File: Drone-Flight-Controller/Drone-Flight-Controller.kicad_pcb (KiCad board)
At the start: 4 copper layers, 30 x 65 mm, 52 parts, among them J1 Screw_Terminal_01x02, J10 Conn_ARM_SWD_TagConnect_TC203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, J2 USB_B_Micro, J3 TestPoint, J4 TestPoint, J5 TestPoint, J6 TestPoint, J7 TestPoint, J8 TestPoint, J9 Raspberry_Pi_4, U1 LMR51430, U4 USBLC6-2SC6, U5 ADC101C021CIMK, U6 MPU-6050, U7 BMP280, U8 STM32F413ZHJx, Y1 16MHz

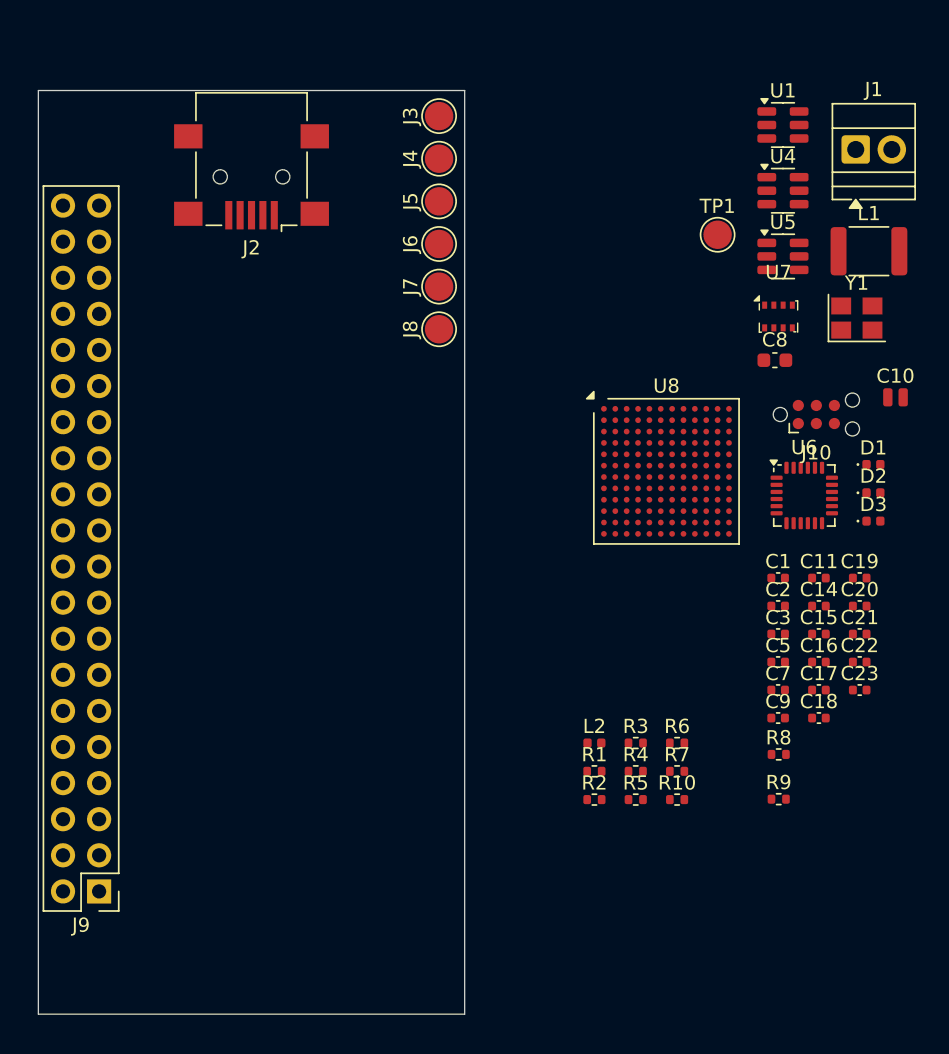
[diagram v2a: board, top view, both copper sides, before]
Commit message: laid out pcb with new mcu
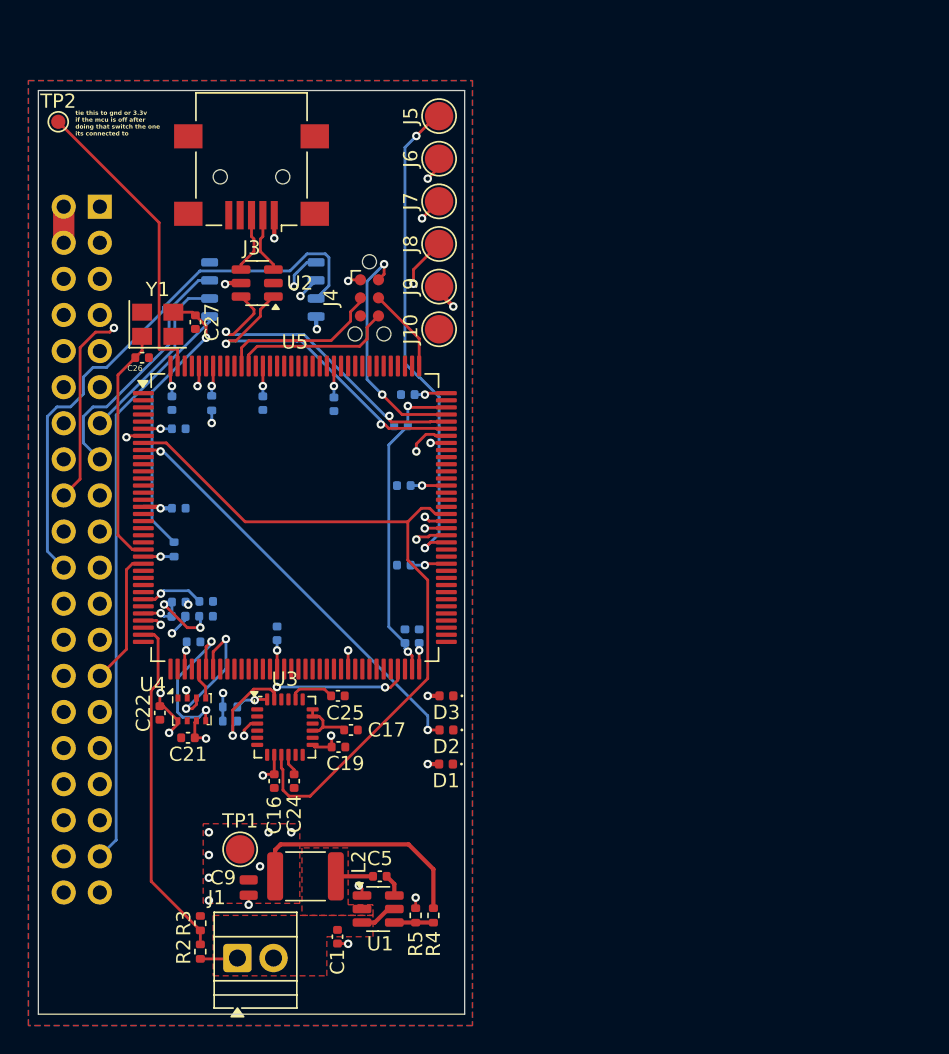
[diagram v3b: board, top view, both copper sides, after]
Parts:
- removed the C1 at (64.3, 46.5)
- removed the C3 at (64.3, 50.5)
- removed the C9 at (64.3, 56.4)
- removed the R1 at (51.3, 60.1)
- removed the R6 at (57.1, 58.1)
- removed the R7 at (57.1, 60.1)
- removed U8: STM32F413ZHJx, Package_BGA:UFBGA-144_10x10mm_Layout12x12_P0.8mm
- added C10: 100n, Capacitor_SMD:C_0402_1005Metric, B.Cu at (37.9, 45.6)
- added C12: 100n, Capacitor_SMD:C_0402_1005Metric, B.Cu at (22.1, 36.0)
- added C13: 100n, Capacitor_SMD:C_0402_1005Metric, B.Cu at (38.2, 33.6)
- added C15: 100n, Capacitor_SMD:C_0402_1005Metric, B.Cu at (37.9, 40.0)
- added C18: 100n, Capacitor_SMD:C_0402_1005Metric, B.Cu at (23.1, 51.0)
- added C20: 100n, Capacitor_SMD:C_0402_1005Metric, B.Cu at (29.0, 50.4)
- added C23: 4.3uF, Capacitor_SMD:C_0402_1005Metric, B.Cu at (24.0, 48.1)
- added C26: 12p, Capacitor_SMD:C_0402_1005Metric, F.Cu at (19.5, 31.0)
- added C27: 12p, Capacitor_SMD:C_0402_1005Metric, F.Cu at (23.2, 28.5)
- added C29: 2.2uF, Capacitor_SMD:C_0402_1005Metric, B.Cu at (37.7, 35.8)
- added C6: 100n, Capacitor_SMD:C_0402_1005Metric, B.Cu at (21.6, 34.2)
- added C7: 100n, Capacitor_SMD:C_0402_1005Metric, B.Cu at (28.0, 34.2)
- added R8: 47, Resistor_SMD:R_0402_1005Metric, B.Cu at (21.8, 44.5)
- added TP2: TestPoint, TestPoint:TestPoint_Pad_D1.0mm, F.Cu at (13.6, 14.4)
- added U3: MPU-9150, Sensor_Motion:InvenSense_QFN-24_4x4mm_P0.5mm, F.Cu at (29.6, 57.0)
- C11, C14: moved to B.Cu
- C2: renamed from C15; moved to B.Cu
- C28: renamed from C5; moved to B.Cu
- C3: renamed from C16; moved to B.Cu
- C8: value 4u7 -> 100n; footprint Capacitor_SMD:C_0603_1608Metric -> Capacitor_SMD:C_0402_1005Metric; moved to B.Cu
- J2: renamed from J9; moved to B.Cu
- L1: renamed from L2; moved to B.Cu
- R1: renamed from R10; moved to B.Cu
- R6: renamed from R8; moved to B.Cu
- R7: renamed from R9; moved to B.Cu
- U5: value ADC101C021CIMK -> STM32F413ZHTx; footprint Package_TO_SOT_SMD:SOT-23-6 -> Package_QFP:LQFP-144_20x20mm_P0.5mm
- U6: value MPU-6050 -> XTSD08G; footprint Sensor_Motion:InvenSense_QFN-24_4x4mm_P0.5mm -> Package_LGA:LGA-8_8x6mm_P1.27mm; moved to B.Cu
- moved J1 71.6 mm to (26.2, 73.2)
- moved U1 62.1 mm to (36.1, 69.8)
- moved L2 59.2 mm to (31.0, 67.5), turned to 180 degrees
- moved C9 57.1 mm to (27.0, 68.3), turned to -90 degrees
- moved TP1 54.8 mm to (26.4, 65.6)
- moved U4 49.7 mm to (23.0, 55.8)
- moved C22 49.3 mm to (20.8, 56.0), turned to 90 degrees
- moved Y1 49.2 mm to (20.6, 28.6)
- moved J2 48.2 mm to (16.5, 20.4)
- moved C21 47.6 mm to (22.7, 57.8), turned to 180 degrees
- moved C11 45.3 mm to (22.1, 41.6)
- moved C2 45.1 mm to (22.1, 48.2)
- moved C3 43.3 mm to (24.0, 49.2)
- moved R1 43.0 mm to (24.4, 34.2), turned to 90 degrees
- moved C24 41.7 mm to (30.2, 60.8), turned to 90 degrees
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- renumbered C2 to C1, C17 to C16, C18 to C17, C22 to C21, C23 to C22, C20 to C24, C21 to C25, C7 to C5, C10 to C9, D3 to D2, D2 to D3, J8 to J10, J2 to J3, J10 to J4, J3 to J5, J4 to J6, J5 to J7, J6 to J8, J7 to J9, L1 to L2, R4 to R2, R5 to R3, R2 to R4, R3 to R5, U4 to U2, U7 to U4
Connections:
- C17 pad 1: Net-(U6-GND) -> Net-(C17-Pad1)
- C24 pad 2: Net-(U6-REGOUT) -> Net-(U3-REGOUT)
- C25 pad 1: Net-(U6-CPOUT) -> Net-(U3-CPOUT)
- C28 pad 2: unconnected-(C5-Pad2) -> Net-(U5-VCAP_1)
- J2 pad 13: unconnected-(J9-GPIO27/SDIO_DAT3-Pad13) -> SD_CARD_DAT3
- J2 pad 15: unconnected-(J9-GPIO22/SDIO_CLK-Pad15) -> SD_CARD_CLK
- J2 pad 16: unconnected-(J9-GPIO23/SDIO_CMD-Pad16) -> SD_CARD_CMD
- J2 pad 18: unconnected-(J9-GPIO24/SDIO_DAT0-Pad18) -> SD_CARD_DAT0
- J2 pad 22: unconnected-(J9-GPIO25/SDIO_DAT1-Pad22) -> SD_CARD_DAT1
- J2 pad 27: unconnected-(J9-ID_SD_I2C0/GPIO00-Pad27) -> NRST
- J2 pad 37: unconnected-(J9-GPIO26/SDIO_DAT2-Pad37) -> SD_CARD_DAT2
- R2 pad 2: Net-(U5-V_{IN}) -> BATVOLTAGE
- R3 pad 1: Net-(U5-V_{IN}) -> BATVOLTAGE
- U5 pad 1: +3.3V -> unconnected-(U5-PE2-Pad1)
- U5 pad 2: GND -> unconnected-(U5-PE3-Pad2)
- U5 pad 3: Net-(U5-V_{IN}) -> unconnected-(U5-PE4-Pad3)
- U5 pad 4: BATVOLTAGE_ADDR -> unconnected-(U5-PE5-Pad4)
- U5 pad 5: BATVOLTAGE_SCL -> unconnected-(U5-PE6-Pad5)
- U5 pad 6: BATVOLTAGE_SDA -> +3.3V
- U6 pad 1: unconnected-(U6-CLKIN-Pad1) -> SD_CARD_DAT2
- U6 pad 2: unconnected-(U6-NC-Pad2) -> SD_CARD_DAT3
- U6 pad 3: unconnected-(U6-NC-Pad3) -> SD_CARD_CLK
- U6 pad 4: unconnected-(U6-NC-Pad4) -> GND
- U6 pad 5: unconnected-(U6-NC-Pad5) -> SD_CARD_CMD
- U6 pad 6: unconnected-(U6-AUX_DA-Pad6) -> SD_CARD_DAT0
- U6 pad 7: unconnected-(U6-AUX_CL-Pad7) -> SD_CARD_DAT1
- Y1 pad 1: Net-(C1-Pad1) -> Net-(U5-PH0)
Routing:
- net IMU_ADDR: track 0.00 -> 52.1 mm
- net +3.3V: track 0.00 -> 49.8 mm, vias 0 -> 26
- net SD_CARD_DAT2: track 0.00 -> 41.2 mm
- net SD_CARD_DAT1: track 0.00 -> 39.9 mm
- net +5V: track 0.00 -> 37.2 mm, vias 0 -> 11
- net PWM_0: track 0.00 -> 34.6 mm, vias 0 -> 2
- net PWM_1: track 0.00 -> 31.6 mm, vias 0 -> 2
- net SD_CARD_CMD: track 0.00 -> 31.3 mm, vias 0 -> 1
- net UART_RX: track 0.00 -> 30.7 mm, vias 0 -> 1
- net UART_TX: track 0.00 -> 30.7 mm, vias 0 -> 1
- net LED_STATUS: track 0.00 -> 29.6 mm, vias 0 -> 2
- net SD_CARD_DAT0: track 0.00 -> 29.4 mm, vias 0 -> 2
- net IMU_SDA: track 0.00 -> 27.5 mm, vias 0 -> 2
- net PWM_2: track 0.00 -> 26.3 mm, vias 0 -> 2
- net BATVOLTAGE: track 0.00 -> 24.3 mm
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- added copper zone on F.Cu, net +12V
- added copper zone on In1.Cu, net +3.3V
- added copper zone on F.Cu, net +5V
- added copper zone on In2.Cu, net +5V
- added copper zone on B.Cu, net GND
- added copper zone on F.Cu, net GND
- added copper zone on F.Cu, net Net-(U1-SW)
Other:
- board text added: "tie this to gnd or 3.3v if the mcu is off after doing that switch the one its connected to"

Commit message: remove stm32
processing will be done on the rpi now
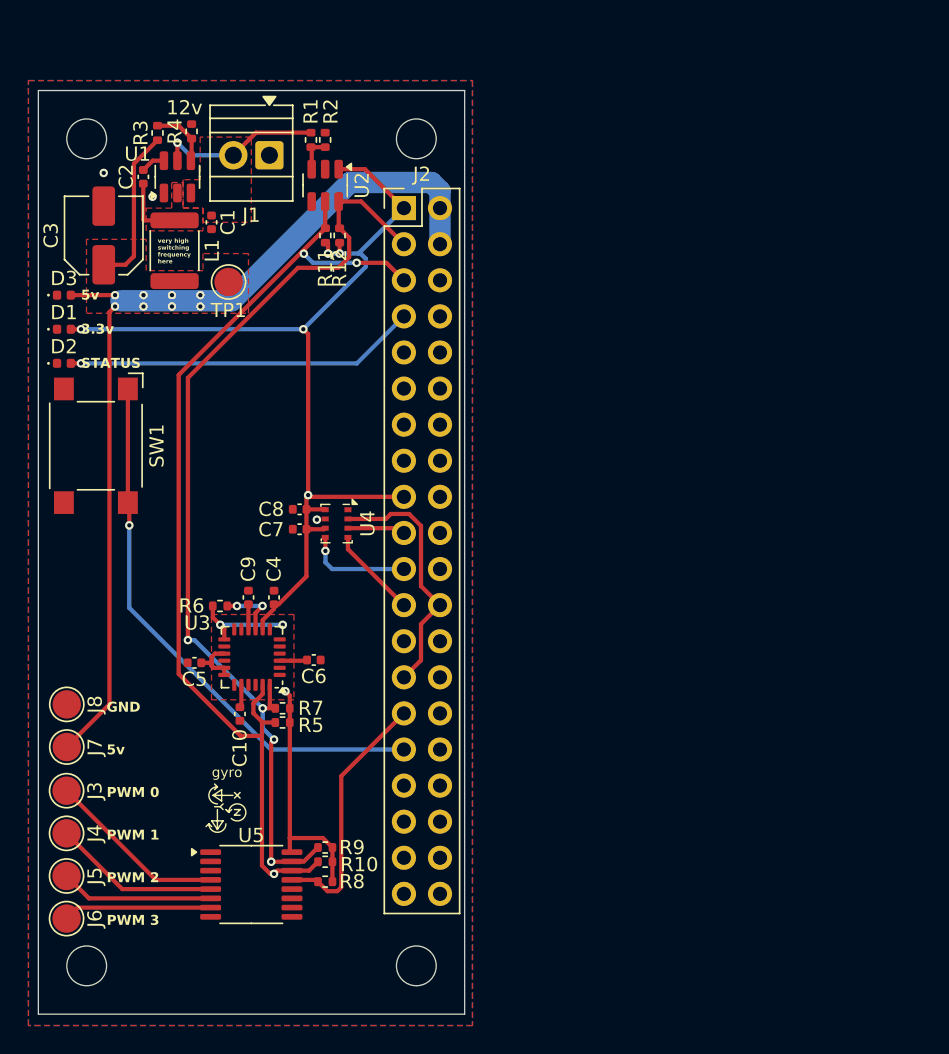
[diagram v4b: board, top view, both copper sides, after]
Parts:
- removed C11, C12, C13, C14, C15, C18, C20: 100n, Capacitor_SMD:C_0402_1005Metric
- removed C16: 10nF, Capacitor_SMD:C_0402_1005Metric
- removed C17, C25: 2.2nF, Capacitor_SMD:C_0402_1005Metric
- removed C19, C24: 0.1uF, Capacitor_SMD:C_0402_1005Metric
- removed C21, C22: 100nF, Capacitor_SMD:C_0402_1005Metric
- removed C23: 4.3uF, Capacitor_SMD:C_0402_1005Metric
- removed C26, C27: 12p, Capacitor_SMD:C_0402_1005Metric
- removed C28, C29: 2.2uF, Capacitor_SMD:C_0402_1005Metric
- removed J10, J9: TestPoint, TestPoint:TestPoint_Pad_D2.0mm
- removed L2: 6.8uH, Inductor_SMD:L_1812_4532Metric
- removed TP2: TestPoint, TestPoint:TestPoint_Pad_D1.0mm
- removed U6: XTSD08G, Package_LGA:LGA-8_8x6mm_P1.27mm
- removed Y1: 16MHz, Crystal:Crystal_SMD_3225-4Pin_3.2x2.5mm
- added C4: 10nF, Capacitor_SMD:C_0402_1005Metric, F.Cu at (28.8, 47.9)
- added R10: 10kOhm, Resistor_SMD:R_0402_1005Metric, F.Cu at (32.4, 66.5)
- added R11: 10kOhm, Resistor_SMD:R_0402_1005Metric, F.Cu at (32.4, 22.4)
- added R12: 10kOhm, Resistor_SMD:R_0402_1005Metric, F.Cu at (33.4, 22.4)
- added R9: 10kOhm, Resistor_SMD:R_0402_1005Metric, F.Cu at (32.4, 65.5)
- added SW1: SW_Omron_B3FS, Button_Switch_SMD:SW_SPST_Omron_B3FS-100xP, F.Cu at (16.2, 37.2)
- C10: value 100n -> 2.2nF; moved to F.Cu
- C2: value 1u -> 0.1uF; moved to F.Cu
- C3: value 10n -> 33uF; footprint Capacitor_SMD:C_0402_1005Metric -> Capacitor_SMD:C_Elec_5x5.4; moved to F.Cu
- C5: value 0.1uF -> 2.2nF
- C6: value 100n -> 0.1uF; moved to F.Cu
- C7, C8: value 100n -> 100nF; moved to F.Cu
- C9: value 33uF -> 0.1uF; footprint Capacitor_SMD:C_0504_1310Metric -> Capacitor_SMD:C_0402_1005Metric
- J2, R6, R7: moved to F.Cu
- J3: value USB_B_Micro -> TestPoint; footprint Connector_USB:USB_Mini-B_Lumberg_2486_01_Horizontal -> TestPoint:TestPoint_Pad_D2.0mm
- J4: value Conn_ARM_SWD_TagConnect_TC2030-NL -> TestPoint; footprint Connector:Tag-Connect_TC2030-IDC-NL_2x03_P1.27mm_Vertical -> TestPoint:TestPoint_Pad_D2.0mm
- L1: value 39n -> 6.8uH; footprint Inductor_SMD:L_0402_1005Metric -> Inductor_SMD:L_1812_4532Metric; moved to F.Cu
- R1: value 10k -> 1.5kOhm; moved to F.Cu
- R2: value 1.5kOhm -> 1kOhm
- R3: value 1kOhm -> 100kOhm
- R4: value 100kOhm -> 13.7kOhm
- R5: value 13.7kOhm -> 10kOhm
- R8: value 47 -> 10kOhm; moved to F.Cu
- U2: value USBLC6-2SC6 -> ADC101C021CIMK
- U5: value STM32F413ZHTx -> PCA9531PW; footprint Package_QFP:LQFP-144_20x20mm_P0.5mm -> Package_SO:TSSOP-16_4.4x5mm_P0.65mm
- moved J5 59.6 mm to (14.2, 67.5), turned to -90 degrees
- moved J6 59.6 mm to (14.2, 70.5), turned to -90 degrees
- moved R2 57.8 mm to (32.4, 15.7)
- moved R4 57.7 mm to (23.0, 15.1), turned to 90 degrees
- moved J1 56.5 mm to (28.5, 16.8), turned to 180 degrees
- moved R3 55.7 mm to (20.6, 15.2)
- moved U1 53.4 mm to (22.0, 18.3), turned to 90 degrees
- moved C1 51.1 mm to (24.4, 21.5)
- moved J7 46.5 mm to (14.2, 58.4), turned to -90 degrees
- moved J3 45.1 mm to (14.2, 61.5), turned to -90 degrees
- moved J4 43.3 mm to (14.2, 64.5)
- moved J8 41.7 mm to (14.2, 55.4), turned to -90 degrees
- moved D1 40.7 mm to (14.0, 29.0), turned to 0 degrees
- moved TP1 39.9 mm to (25.6, 25.7), turned to 180 degrees
- moved D3 39.0 mm to (14.0, 26.6), turned to 0 degrees
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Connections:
- C10 pad 1: +3.3V -> Net-(U3-CPOUT)
- C2 pad 1: +3.3VA -> Net-(U1-CB)
- C2 pad 2: GND -> Net-(U1-SW)
- C3 pad 1: +3.3VA -> +5V
- C5 pad 1: Net-(U1-CB) -> Net-(C5-Pad1)
- C5 pad 2: Net-(U1-SW) -> GND
- C6 pad 1: +3.3V -> GND
- C6 pad 2: GND -> +3.3V
- C8 pad 1: +3.3V -> GND
- C8 pad 2: GND -> +3.3V
- C9 pad 1: +5V -> GND
- C9 pad 2: GND -> Net-(U3-REGOUT)
- J1 pad 1: +12V -> GND
- J1 pad 2: GND -> +12V
- J2 pad 10: UART_RX -> unconnected-(J2-GPIO15/UART_RXD-Pad10)
- J2 pad 13: SD_CARD_DAT3 -> unconnected-(J2-GPIO27/SDIO_DAT3-Pad13)
- J2 pad 15: SD_CARD_CLK -> unconnected-(J2-GPIO22/SDIO_CLK-Pad15)
- J2 pad 16: SD_CARD_CMD -> unconnected-(J2-GPIO23/SDIO_CMD-Pad16)
- J2 pad 18: SD_CARD_DAT0 -> unconnected-(J2-GPIO24/SDIO_DAT0-Pad18)
- J2 pad 19: unconnected-(J2-MOSI_SPI0/GPIO10-Pad19) -> BAROMETER_SDI
- J2 pad 21: unconnected-(J2-MISO_SPI0/GPIO09-Pad21) -> BAROMETER_SDO
- J2 pad 22: SD_CARD_DAT1 -> unconnected-(J2-GPIO25/SDIO_DAT1-Pad22)
- J2 pad 23: unconnected-(J2-SCLK_SPI0/GPIO11-Pad23) -> BAROMETER_SCK
- J2 pad 24: unconnected-(J2-~{CE0}_SPI0/GPIO08-Pad24) -> BAROMETER_CSB
- J2 pad 27: NRST -> BAROMETER_CSB
- J2 pad 28: unconnected-(J2-ID_SC_I2C0/GPIO01-Pad28) -> IMU_ADDR
- J2 pad 29: unconnected-(J2-GPCLK1/GPIO05-Pad29) -> PWM_RESET
- J2 pad 3: unconnected-(J2-SDA_I2C1/GPIO02-Pad3) -> I2C_SDA
- J2 pad 31: unconnected-(J2-GPCLK2/GPIO06-Pad31) -> Net-(J2-GPCLK2/GPIO06)
- J2 pad 37: SD_CARD_DAT2 -> unconnected-(J2-GPIO26/SDIO_DAT2-Pad37)
- J2 pad 5: unconnected-(J2-SCL_I2C1/GPIO03-Pad5) -> I2C_SCL
- J2 pad 7: unconnected-(J2-GPCLK0/GPIO04-Pad7) -> LED_STATUS
- J2 pad 8: UART_TX -> unconnected-(J2-GPIO14/UART_TXD-Pad8)
- J3 pad 1: +5V -> PWM_0
- J4 pad 1: +3.3V -> PWM_1
- J5 pad 1: PWM_0 -> PWM_2
- J6 pad 1: PWM_1 -> PWM_3
- J7 pad 1: PWM_2 -> +5V
- J8 pad 1: PWM_3 -> GND
- L1 pad 1: +3.3V -> Net-(U1-SW)
- L1 pad 2: +3.3VA -> +5V
- R1 pad 1: +3.3V -> +12V
- R1 pad 2: BOOT0 -> BATVOLTAGE
- R2 pad 1: +12V -> BATVOLTAGE
- R2 pad 2: BATVOLTAGE -> GND
- R3 pad 1: BATVOLTAGE -> +5V
- R3 pad 2: GND -> Net-(U1-FB)
- R4 pad 1: +5V -> Net-(U1-FB)
- R4 pad 2: Net-(U1-FB) -> GND
- R5 pad 1: Net-(U1-FB) -> +3.3V
- R5 pad 2: GND -> I2C_SCL
- R6 pad 1: +3.3V -> Net-(U3-AD0)
- R6 pad 2: IMU_SCL -> +3.3V
- R7 pad 2: IMU_SDA -> I2C_SDA
- R8 pad 1: Net-(U5-PH1) -> +3.3V
- R8 pad 2: Net-(C27-Pad1) -> PWM_RESET
- U2 pad 1: USB_D- -> +3.3V
- U2 pad 3: USB_CONN_D- -> BATVOLTAGE
- U2 pad 4: USB_CONN_D+ -> GND
- U2 pad 5: +5V -> I2C_SCL
- U2 pad 6: USB_D+ -> I2C_SDA
- U3 pad 15: Net-(C17-Pad1) -> Net-(C5-Pad1)
- U3 pad 17: Net-(C17-Pad1) -> Net-(C5-Pad1)
- U3 pad 18: Net-(C17-Pad1) -> Net-(C5-Pad1)
- U3 pad 23: IMU_SCL -> I2C_SCL
- U3 pad 24: IMU_SDA -> I2C_SDA
- U3 pad 9: IMU_ADDR -> Net-(U3-AD0)
- U5 pad 1: unconnected-(U5-PE2-Pad1) -> GND
- U5 pad 13: unconnected-(U5-PF3-Pad13) -> PWM_RESET
- U5 pad 14: unconnected-(U5-PF4-Pad14) -> I2C_SCL
- U5 pad 15: unconnected-(U5-PF5-Pad15) -> I2C_SDA
- U5 pad 16: GND -> +3.3V
- U5 pad 2: unconnected-(U5-PE3-Pad2) -> GND
- U5 pad 3: unconnected-(U5-PE4-Pad3) -> GND
- U5 pad 4: unconnected-(U5-PE5-Pad4) -> PWM_0
- U5 pad 5: unconnected-(U5-PE6-Pad5) -> PWM_1
- U5 pad 6: +3.3V -> PWM_2
- U5 pad 7: BAROMETER_CSB -> PWM_3
- U5 pad 8: IMU_ADDR -> GND
- U5 pad 9: LED_STATUS -> unconnected-(U5-LED4-Pad9)
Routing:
- net I2C_SCL: track 0.00 -> 71.9 mm, vias 0 -> 3
- net I2C_SDA: track 0.00 -> 68.2 mm, vias 0 -> 4
- net IMU_ADDR: track 52.1 -> 0.00 mm
- net +3.3V: track 49.8 -> 96.4 mm, vias 26 -> 8
- net SD_CARD_DAT2: track 41.2 -> 0.00 mm
- net SD_CARD_DAT1: track 39.9 -> 0.00 mm
- net +5V: track 37.2 -> 76.7 mm, vias 11 -> 8
- net Net-(J2-GPCLK2/GPIO06): track 0.00 -> 38.9 mm, vias 0 -> 1
- net SD_CARD_CMD: track 31.3 -> 0.00 mm, vias 1 -> 0
- net UART_RX: track 30.7 -> 0.00 mm, vias 1 -> 0
- net UART_TX: track 30.7 -> 0.00 mm, vias 1 -> 0
- net SD_CARD_DAT0: track 29.4 -> 0.00 mm, vias 2 -> 0
- net IMU_SDA: track 27.5 -> 0.00 mm, vias 2 -> 0
- net USB_D-: track 23.3 -> 0.00 mm, vias 2 -> 0
- net USB_D+: track 22.6 -> 0.00 mm, vias 2 -> 0
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- added copper zone on F.Cu, net +3.3V
- removed copper zone on In1.Cu, net +3.3V
- removed copper zone on In2.Cu, net +5V
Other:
- outline, holes or cut-outs redrawn
- copper layers 4 -> 2
- board text added: "12v"
- board text added: "3.3v"
- board text added: "5v"
- board text added: "GND"
- board text added: "PWM 0"
- board text added: "PWM 1"
- board text added: "PWM 2"
- board text added: "PWM 3"
- board text added: "STATUS"
- board text added: "gyro"
- board text added: "very high switching frequency here"
- board text removed: "tie this to gnd or 3.3v if the mcu is off after doing that switch the one its connected to"

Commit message: pin header is female and on the bottom now
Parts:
- added J10: TestPoint, TestPoint:TestPoint_Pad_D2.0mm, F.Cu at (22.0, 75.2)
- added J11: TestPoint, TestPoint:TestPoint_Pad_D2.0mm, F.Cu at (25.0, 75.2)
- added J12: TestPoint, TestPoint:TestPoint_Pad_D2.0mm, F.Cu at (28.0, 75.2)
- added J9: TestPoint, TestPoint:TestPoint_Pad_D2.0mm, F.Cu at (19.0, 75.2)
- J2: footprint Connector_PinHeader_2.54mm:PinHeader_2x20_P2.54mm_Vertical -> Connector_PinSocket_2.54mm:PinSocket_2x20_P2.54mm_Vertical; moved to B.Cu
- turned J2 to 180 degrees
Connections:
- U5 pad 10: unconnected-(U5-LED5-Pad10) -> PWM_5
- U5 pad 11: unconnected-(U5-LED6-Pad11) -> PWM_6
- U5 pad 12: unconnected-(U5-LED7-Pad12) -> PWM_7
- U5 pad 9: unconnected-(U5-LED4-Pad9) -> PWM_4
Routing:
- net PWM_4: track 0.00 -> 13.1 mm
- net PWM_5: track 0.00 -> 12.8 mm
- net PWM_6: track 0.00 -> 11.4 mm
- net PWM_7: track 0.00 -> 9.88 mm
- net GND: vias 3 -> 12
- net +5V: vias 8 -> 11
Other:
- board text added: "0"
- board text added: "1"
- board text added: "2"
- board text added: "3"
- board text added: "4"
- board text added: "5"
- board text added: "6"
- board text added: "7"
- board text added: "PWM"
- board text removed: "PWM 0"
- board text removed: "PWM 1"
- board text removed: "PWM 2"
- board text removed: "PWM 3"

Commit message: change imu to one that isnt eol
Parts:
- removed the C10 at (26.4, 56.1)
- removed the C4 at (28.8, 47.9)
- removed the C5 at (23.2, 52.5)
- removed the R5 at (29.4, 56.7)
- removed the R6 at (25.0, 48.5)
- removed the U3 at (27.2, 52.1)
- added C2: 1uF, Capacitor_SMD:C_0402_1005Metric, F.Cu at (25.8, 45.4)
- added C3: 1uF, Capacitor_SMD:C_0402_1005Metric, F.Cu at (25.8, 47.4)
- added C7: 0.1uF, Capacitor_SMD:C_0402_1005Metric, F.Cu at (26.0, 54.8)
- added F1: Fuse, Fuse:Fuse_1206_3216Metric, F.Cu at (24.0, 8.80)
- added U1: MCP1700x-180xxMB, Package_TO_SOT_SMD:SOT-89-3, F.Cu at (29.2, 46.4)
- added U4: ICM-20948, Sensor_Motion:InvenSense_QFN-24_3x3mm_P0.4mm, F.Cu at (27.2, 52.1)
- moved C6 7.60 mm to (24.4, 49.8), turned to -90 degrees
- moved C9 6.46 mm to (24.4, 53.8)
- moved R7 6.31 mm to (24.4, 51.8), turned to 90 degrees
- moved R4 0.75 mm to (22.8, 15.8), turned to 0 degrees
- moved R3 0.69 mm to (20.9, 15.8), turned to 0 degrees
- moved C4 0.22 mm to (19.4, 18.4)
- moved U2 0.13 mm to (22.0, 18.4)
- moved C1 0.08 mm to (24.4, 21.4)
- renumbered C8 to C10, C2 to C4, C3 to C5, C7 to C8, J7 to J3, J8 to J4, J3 to J5, J4 to J6, J5 to J7, J6 to J8, R12 to R5, R11 to R6, U1 to U2, U2 to U3, U4 to U5, U5 to U6
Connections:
- C6 pad 2: +3.3V -> +1V8
- C9 pad 1: GND -> Net-(U4-REGOUT)
- C9 pad 2: Net-(U3-REGOUT) -> GND
- J1 pad 2: +12V -> Net-(J1-Pin_2)
- R7 pad 1: +3.3V -> Net-(U4-SDO/AD0)
- R7 pad 2: I2C_SDA -> +1V8
- U3 pad 4: GND -> unconnected-(U3-ADDR-Pad4)
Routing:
- net +1V8: track 0.00 -> 10.8 mm, vias 0 -> 2
- net I2C_SDA: track 68.2 -> 74.2 mm, vias 4 -> 3
- net +12V: track 11.7 -> 6.12 mm, vias 1 -> 0
- net GND: track 0.00 -> 5.39 mm, vias 12 -> 14
- net Net-(U3-AD0): track 4.13 -> 0.00 mm, vias 2 -> 0
- net Net-(C5-Pad1): track 3.79 -> 0.00 mm
- net I2C_SCL: track 71.9 -> 75.3 mm
- net Net-(U4-REGOUT): track 0.00 -> 1.77 mm
- net Net-(U3-REGOUT): track 1.77 -> 0.00 mm
- net Net-(U2-FB): track 4.35 -> 2.63 mm
- net Net-(U3-CPOUT): track 1.61 -> 0.00 mm
- net +3.3V: track 96.4 -> 94.8 mm, vias 8 -> 5
- net Net-(U4-SDO/AD0): track 0.00 -> 1.47 mm
- net +5V: track 76.7 -> 75.6 mm
- added copper zone on F.Cu, net +1V8
- removed copper zone on F.Cu, net +3.3V
